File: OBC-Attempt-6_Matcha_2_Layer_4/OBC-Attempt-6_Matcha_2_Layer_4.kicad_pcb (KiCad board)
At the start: 2 copper layers, 57.1 x 57.1 mm, 59 parts, among them J2 Screw_Terminal_01x08, J3 Screw_Terminal_01x08, J5 Conn_01x04, J6 Micro_SD_Card, J7 Screw_Terminal_01x02, J8 Screw_Terminal_01x02, SW1 PCM12SMTR, U1 BMI088, U10 CPC1020NTR, U11 CPC1020NTR, U12 NCP1117-3.3_SOT223, U2 CPC1020NTR, U3 CPC1020NTR, U4 CPC1020NTR, U5 CPC1020NTR, U7 CPC1020NTR, U8 CPC1020NTR, U9 STM32F401RDTx, Y1 ABMM2-25MHZ-D1-T

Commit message: Some Changes
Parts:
- removed D5, D6, D7, D8: B330, Diode_SMD:D_SMA
- removed J3: Screw_Terminal_01x08, TerminalBlock_Phoenix:TerminalBlock_Phoenix_MPT-0,5-8-2.54_1x08_P2.54mm_Horizontal
- removed R14, R15, R16, R17: 270, Resistor_SMD:R_0603_1608Metric
- removed U10, U11, U7, U8: CPC1020NTR, CPC1020NTR:4-SOP
- moved J7 38.9 mm to (29.2, 58.4), turned to 90 degrees
- moved BZ1 36.1 mm to (38.0, 49.9), turned to -45 degrees
- moved J2 33.4 mm to (59.5, 72.4), turned to 180 degrees
- moved D4 30.9 mm to (62.4, 69.1), turned to 180 degrees
- moved D1 30.7 mm to (40.9, 69.0), turned to 180 degrees
- moved D3 27.4 mm to (55.2, 69.1), turned to 180 degrees
- moved D2 27.3 mm to (48.0, 69.1), turned to 180 degrees
- moved U4 25.2 mm to (63.1, 63.5), turned to 180 degrees
- moved U1 23.5 mm to (41.6, 63.4), turned to 180 degrees
- moved J8 23.1 mm to (29.2, 50.8), turned to 90 degrees
- moved Y1 21.8 mm to (39.0, 29.6), turned to -135 degrees
- moved R12 21.7 mm to (64.4, 58.3), turned to 90 degrees
- moved C20 20.3 mm to (26.8, 41.8), turned to 90 degrees
- moved U3 20.2 mm to (56.1, 63.5), turned to 180 degrees
- moved U2 19.5 mm to (48.8, 63.5), turned to 180 degrees
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- renumbered D3 to D2, D4 to D3, D2 to D4, U4 to U1, U5 to U4, U1 to U5, U9 to U6
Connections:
- C20 pad 1: BATT+ -> PWR
- J5 pad 2: 3.3V -> SYS_JTMS-SWDIO
- J5 pad 3: SYS_JTMS-SWDIO -> 3.3V
- J7 pad 1: BATT+ -> GND
- J7 pad 2: GND -> BATT+
- J8 pad 1: PWR -> BATT+
- J8 pad 2: BATT+ -> PWR
- R18 pad 1: BATT+ -> PWR
- U12 pad 3: BATT+ -> PWR
- U6 pad 24: SOL1 -> BUZZER
- U6 pad 25: SOL3 -> unconnected-(U6-Pad25)
- U6 pad 26: SOL2 -> unconnected-(U6-Pad26)
- U6 pad 27: SOL4 -> unconnected-(U6-Pad27)
- U6 pad 41: SOL5 -> SOL1
- U6 pad 42: SOL7 -> SOL2
- U6 pad 43: SOL6 -> SOL3
- U6 pad 44: SOL8 -> SOL4
- U6 pad 56: BUZZER -> unconnected-(U6-Pad56)
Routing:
- net PWR: track 91.8 -> 58.2 mm
- net SOL8: track 22.3 -> 0.00 mm, vias 2 -> 0
- net SOL5: track 22.0 -> 0.00 mm, vias 2 -> 0
- net SOL7: track 18.6 -> 0.00 mm, vias 2 -> 0
- net SOL6: track 16.6 -> 0.00 mm, vias 2 -> 0
- net SOL1: track 10.6 -> 25.2 mm
- net Net-(D8-Pad1): track 8.85 -> 0.00 mm
- net GND: track 57.9 -> 49.3 mm, vias 46 -> 33
- net SOL2: track 11.8 -> 19.8 mm
- net BATT+: track 12.8 -> 5.08 mm
- net Net-(D7-Pad1): track 7.00 -> 0.00 mm
- net Net-(D6-Pad1): track 6.80 -> 0.00 mm
- net VMON: track 20.7 -> 14.1 mm
- net Net-(D5-Pad1): track 6.11 -> 0.00 mm
- net RCC_OSC_OUT: track 5.70 -> 11.3 mm
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- added copper zone on F.Cu, net PWR
- removed copper zone on F.Cu, net BATT+
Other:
- board size 57.1 x 57.1 mm -> 50.8 x 50.8 mm
- board text added: "-BATT IN+"
- board text added: "GND"
- board text added: "MATCHA V2.0"
- board text removed: "+BATT IN-"
- board text removed: "+SOL5-"
- board text removed: "+SOL6-"
- board text removed: "+SOL7-"
- board text removed: "+SOL8-"
- board text removed: "G"
- board text removed: "MATCHA V3.0"

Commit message: PCB LAYOUT
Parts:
- removed BZ1: Buzzer, Buzzer_Beeper:Buzzer_TDK_PS1240P02BT_D12.2mm_H6.5mm
- removed C1, C11, C13, C2, C3, C4, C6, C8, C9: 100nF, Capacitor_SMD:C_0402_1005Metric
- removed C10: 1uF, Capacitor_SMD:C_0603_1608Metric
- removed C15: 4.7uF, Capacitor_SMD:C_0603_1608Metric
- removed C16, C17: 26pf, Capacitor_SMD:C_0402_1005Metric
- removed C20: 100nF, Capacitor_SMD:C_0603_1608Metric
- removed C21: 10uF, Capacitor_SMD:C_0603_1608Metric
- removed C7: 4.7uF, Capacitor_SMD:C_0402_1005Metric
- removed D1, D2, D3, D4: B330, Diode_SMD:D_SMA
- removed H1, H2, H3, H4: MountingHole, MountingHole:MountingHole_3mm
- removed J2: Screw_Terminal_01x08, TerminalBlock_Phoenix:TerminalBlock_Phoenix_MPT-0,5-8-2.54_1x08_P2.54mm_Horizontal
- removed J5: Conn_01x04, Connector_PinHeader_2.54mm:PinHeader_1x04_P2.54mm_Vertical
- removed J6: Micro_SD_Card, Connector_Card:microSD_HC_Wuerth_693072010801
- removed J7, J8: Screw_Terminal_01x02, TerminalBlock_Phoenix:TerminalBlock_Phoenix_MPT-0,5-2-2.54_1x02_P2.54mm_Horizontal
- removed R10, R11, R12, R9: 270, Resistor_SMD:R_0603_1608Metric
- removed R13: 10k, Resistor_SMD:R_0603_1608Metric
- removed R18: 1M, Resistor_SMD:R_0603_1608Metric
- removed R19: 100K, Resistor_SMD:R_0603_1608Metric
- removed SW1: PCM12SMTR, PCM12SMTR:SW_PCM12SMTR
- removed U1, U2, U3, U4: CPC1020NTR, CPC1020NTR:4-SOP
- removed U12: NCP1117-3.3_SOT223, Package_TO_SOT_SMD:SOT-223-3_TabPin2
- removed U5: BMI088, BMI088:BMI088
- removed U6: STM32F401RDTx, Package_QFP:LQFP-64_10x10mm_P0.5mm
- removed Y1: ABMM2-25MHZ-D1-T, ABMM2_6mm_3_6mm:XTAL_ABMM2-25.000MHZ-D1-T
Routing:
- net 3.3V: track 93.2 -> 0.00 mm, vias 4 -> 0
- net PWR: track 58.2 -> 0.00 mm
- net GND: track 49.3 -> 0.00 mm, vias 33 -> 0
- net SDIO_CK: track 29.7 -> 0.00 mm
- net SDIO_D0: track 27.0 -> 0.00 mm
- net SOL1: track 25.2 -> 0.00 mm, vias 2 -> 0
- net SDIO_D3: track 23.8 -> 0.00 mm
- net SDIO_CMD: track 22.7 -> 0.00 mm
- net SOL4: track 22.1 -> 0.00 mm, vias 2 -> 0
- net SDIO_D1: track 21.7 -> 0.00 mm
- net SOL2: track 19.8 -> 0.00 mm, vias 2 -> 0
- net SDIO_D2: track 19.6 -> 0.00 mm
- net MISO: track 19.1 -> 0.00 mm
- net CS2_GYRO: track 19.0 -> 0.00 mm
- net SOL3: track 17.1 -> 0.00 mm, vias 2 -> 0
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- removed copper zone on F.Cu, net 3.3V
- removed copper zone on B.Cu, net GND
- removed copper zone on F.Cu, net GND
- removed copper zone on F.Cu, net PWR
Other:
- board outline removed
- board text removed: "+SOL1-"
- board text removed: "+SOL2-"
- board text removed: "+SOL3-"
- board text removed: "+SOL4-"
- board text removed: "- RCS"
- board text removed: "-BATT IN+"
- board text removed: "3.3"
- board text removed: "ALEX AARHUS"
- board text removed: "ARM"
- board text removed: "BOOT0"
- board text removed: "CLK"
- board text removed: "DIO"
- board text removed: "GND"
- board text removed: "GO KARMAN!"
- board text removed: "GO SAN DIEGO!"
- board text removed: "MATCHA V2.0"
- board text removed: "PSHHHHHHHHH!"
- board text removed: "SDSURP 2023"

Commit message: Complete chematic
Might have to change the optocouplers
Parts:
- added C1: 4.7nF, Capacitor_SMD:C_0402_1005Metric, F.Cu at (157.6, 59.0)
- added C2: 20pF, Capacitor_SMD:C_0402_1005Metric, F.Cu at (159.6, 84.3)
- added C20: 100nF, Capacitor_SMD:C_0603_1608Metric, F.Cu at (139.0, 73.7)
- added C21: 10uF, Capacitor_SMD:C_0603_1608Metric, F.Cu at (145.0, 66.2)
- added C3: 20pF, Capacitor_SMD:C_0402_1005Metric, F.Cu at (159.5, 86.2)
- added C4: 4u7, Capacitor_SMD:C_0402_1005Metric, F.Cu at (165.9, 87.0)
- added C5: 1uF, Capacitor_SMD:C_0402_1005Metric, F.Cu at (166.4, 85.6)
- added C6: .1uF, Capacitor_SMD:C_0402_1005Metric, F.Cu at (136.0, 79.5)
- added C7: 10nF, Capacitor_SMD:C_0402_1005Metric, F.Cu at (152.8, 63.5)
- added D1: CVJ10F30, CVJ10F30:CVJ10F30, F.Cu at (164.4, 39.4)
- added D2: CVJ10F30, CVJ10F30:CVJ10F30, F.Cu at (157.2, 62.1)
- added H1: MountingHole_Pad, MountingHole:MountingHole_2.2mm_M2_Pad_TopBottom, F.Cu at (128.4, 75.5)
- added H2: MountingHole_Pad, MountingHole:MountingHole_2.2mm_M2_Pad_TopBottom, F.Cu at (140.0, 65.0)
- added H3: MountingHole_Pad, MountingHole:MountingHole_2.2mm_M2_Pad_TopBottom, F.Cu at (143.3, 59.0)
- added H4: MountingHole_Pad, MountingHole:MountingHole_2.2mm_M2_Pad_TopBottom, F.Cu at (124.6, 81.4)
- added J1: CAN Header, Connector_PinHeader_1.00mm:PinHeader_1x04_P1.00mm_Vertical, F.Cu at (138.7, 57.5)
- added J2: SOL A, TerminalBlock_Phoenix:TerminalBlock_Phoenix_MPT-0,5-4-2.54_1x04_P2.54mm_Horizontal, F.Cu at (170.0, 44.9)
- added J3: SOL B, TerminalBlock_Phoenix:TerminalBlock_Phoenix_MPT-0,5-4-2.54_1x04_P2.54mm_Horizontal, F.Cu at (103.9, 83.6)
- added J5: Conn_01x04, Connector_PinHeader_2.54mm:PinHeader_1x04_P2.54mm_Vertical, F.Cu at (166.6, 80.9)
- added J7: Screw_Terminal_01x02, TerminalBlock_Phoenix:TerminalBlock_Phoenix_MPT-0,5-2-2.54_1x02_P2.54mm_Horizontal, F.Cu at (116.5, 83.6)
- added J8: Screw_Terminal_01x02, TerminalBlock_Phoenix:TerminalBlock_Phoenix_MPT-0,5-2-2.54_1x02_P2.54mm_Horizontal, F.Cu at (130.1, 68.4)
- added R1: 60 ohm, Resistor_SMD:R_0805_2012Metric, F.Cu at (116.7, 78.0)
- added R10: R, Resistor_SMD:R_0603_1608Metric, F.Cu at (128.0, 85.7)
- added R11: R, Resistor_SMD:R_0603_1608Metric, F.Cu at (149.4, 61.7)
- added R18: 1M, Resistor_SMD:R_0603_1608Metric, F.Cu at (149.4, 64.2)
- added R19: 100K, Resistor_SMD:R_0603_1608Metric, F.Cu at (143.0, 69.3)
- added R2: 60 ohm, Resistor_SMD:R_0805_2012Metric, F.Cu at (145.2, 63.4)
- added R3: 10k, Resistor_SMD:R_0402_1005Metric, F.Cu at (138.5, 76.0)
- added R4: R, Resistor_SMD:R_0402_1005Metric, F.Cu at (144.8, 38.8)
- added R5: R, Resistor_SMD:R_0402_1005Metric, F.Cu at (144.7, 43.8)
- added R6: R, Resistor_SMD:R_0402_1005Metric, F.Cu at (157.6, 57.0)
- added R7: R, Resistor_SMD:R_0402_1005Metric, F.Cu at (142.5, 71.5)
- added R8: R, Resistor_SMD:R_0603_1608Metric, F.Cu at (158.8, 40.4)
- added R9: R, Resistor_SMD:R_0603_1608Metric, F.Cu at (158.8, 45.5)
- added SW1: SW_SPST, Jumper:SolderJumper-2_P1.3mm_Open_RoundedPad1.0x1.5mm, F.Cu at (123.8, 86.2)
- added SW2: SW_SPDT, Jumper:SolderJumper-3_P1.3mm_Open_RoundedPad1.0x1.5mm_NumberLabels, F.Cu at (134.2, 74.3)
- added U1: LTV-827S, Package_DIP:SMDIP-8_W9.53mm, F.Cu at (151.9, 42.5)
- added U12: NCP1117-3.3_SOT223, Package_TO_SOT_SMD:SOT-223-3_TabPin2, F.Cu at (132.1, 60.1)
- added U2: LTV-827S, Package_DIP:SMDIP-8_W9.53mm, F.Cu at (107.9, 73.6)
- added U3: QS5K2TR, QS5K2TR:SOT95P280X100-5N, F.Cu at (161.8, 42.2)
- added U4: QS5K2TR, QS5K2TR:SOT95P280X100-5N, F.Cu at (149.5, 58.2)
- added U5: SN65HVD230, Package_SO:SOIC-8_3.9x4.9mm_P1.27mm, F.Cu at (123.4, 67.5)
- added U6: STM32F042G4Ux, Package_DFN_QFN:QFN-28_4x4mm_P0.5mm, F.Cu at (162.8, 86.0)
- added X1: ECS-2520MV-xxx-xx, Oscillator:Oscillator_SMD_ECS_2520MV-xxx-xx-4Pin_2.5x2.0mm, F.Cu at (157.7, 85.0)
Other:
- board outline added: 50.8 x 50.8 mm

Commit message: Some late night pcb work
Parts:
- removed J7, J8: Screw_Terminal_01x02, TerminalBlock_Phoenix:TerminalBlock_Phoenix_MPT-0,5-2-2.54_1x02_P2.54mm_Horizontal
- removed U2: LTV-827S, Package_DIP:SMDIP-8_W9.53mm
- added J4: Screw_Terminal_01x04, TerminalBlock_Phoenix:TerminalBlock_Phoenix_MPT-0,5-4-2.54_1x04_P2.54mm_Horizontal, B.Cu at (34.2, 29.0)
- D1, D2, J2, J3, R10, R11, R4, R5, R6, R7, R8, R9, U3, U4: moved to B.Cu
- J5: footprint Connector_PinHeader_2.54mm:PinHeader_1x04_P2.54mm_Vertical -> Connector_PinHeader_1.00mm:PinHeader_1x04_P1.00mm_Vertical; moved to B.Cu
- U1: value LTV-827S -> LTV-247; footprint Package_DIP:SMDIP-8_W9.53mm -> Package_SO:SOP-16_4.4x10.4mm_P1.27mm; moved to B.Cu
- moved C1 144.5 mm to (13.9, 43.4), turned to 180 degrees
- moved D1 133.9 mm to (31.3, 54.4), turned to -90 degrees
- moved R2 132.3 mm to (14.7, 41.9)
- moved J2 129.2 mm to (41.7, 60.0), turned to 180 degrees
- moved C4 129.1 mm to (44.0, 44.5)
- moved U3 128.8 mm to (33.3, 51.8), turned to -90 degrees
- moved C5 128.1 mm to (45.0, 44.5), turned to -90 degrees
- moved R8 128.0 mm to (31.1, 48.5), turned to 0 degrees
- moved U6 126.1 mm to (45.0, 40.9), turned to -90 degrees
- moved R9 124.8 mm to (34.1, 48.5), turned to 0 degrees
- moved C3 124.8 mm to (45.0, 36.7), turned to 180 degrees
- moved J5 123.9 mm to (49.5, 40.5), turned to 180 degrees
- moved R6 122.8 mm to (36.1, 38.6), turned to 90 degrees
- moved X1 122.3 mm to (46.2, 34.7), turned to -90 degrees
- moved C2 122.1 mm to (46.7, 37.7), turned to 0 degrees
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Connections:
- U1 pad 5: Net-(R9-Pad2) -> Net-(R6-Pad1)
- U1 pad 6: PWR -> GND
- U1 pad 7: Net-(R8-Pad2) -> Net-(R7-Pad1)
- U1 pad 8: PWR -> GND
- U5 pad 3: +3.3V -> 3.3V
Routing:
- net GND: vias 0 -> 2
- net 3.3V: vias 0 -> 4
- added copper zone on F.Cu, net 3.3V
- added copper zone on In2.Cu, net 3.3V
- added copper zone on F.Cu, net BATT+
- added copper zone on F.Cu, net GND
- added copper zone on In1.Cu, net GND
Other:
- board size 50.8 x 50.8 mm -> 25.4 x 38.1 mm
- copper layers 2 -> 4

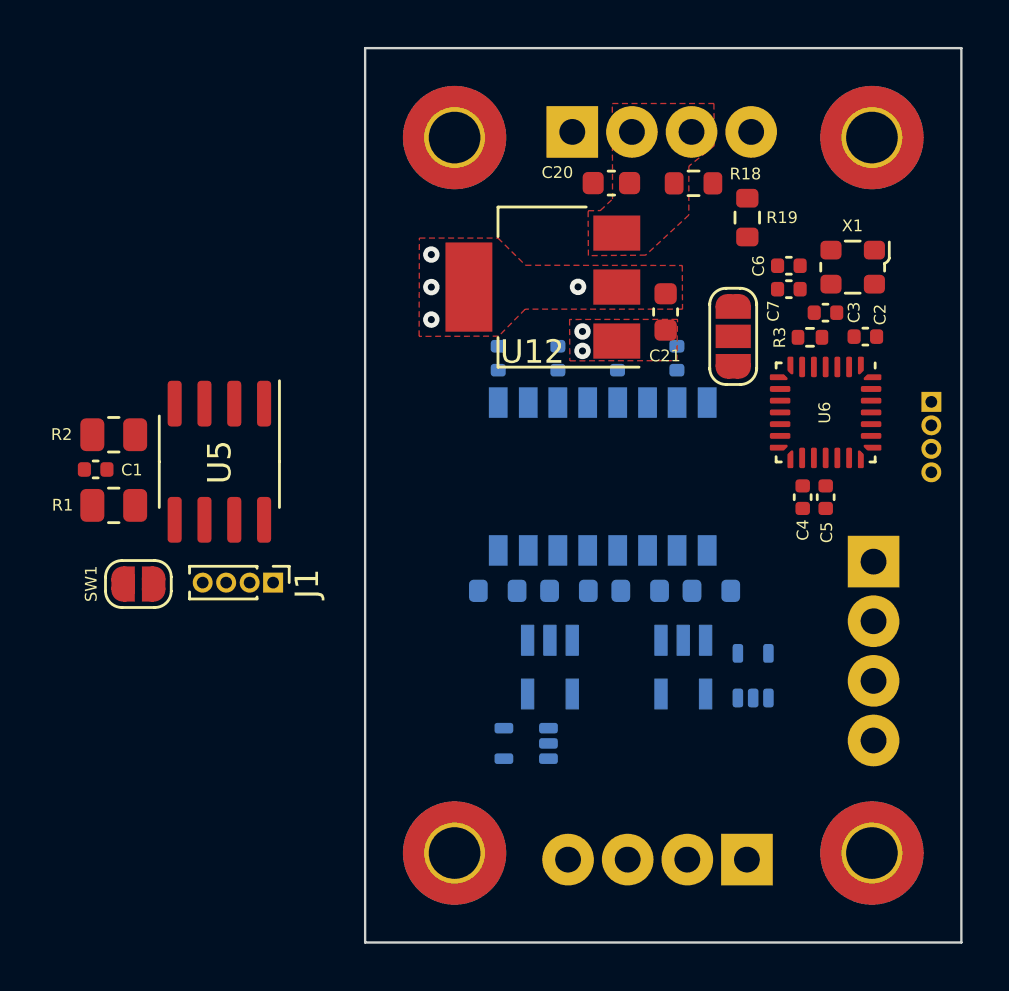
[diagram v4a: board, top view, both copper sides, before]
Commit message: Wired Everything in the board
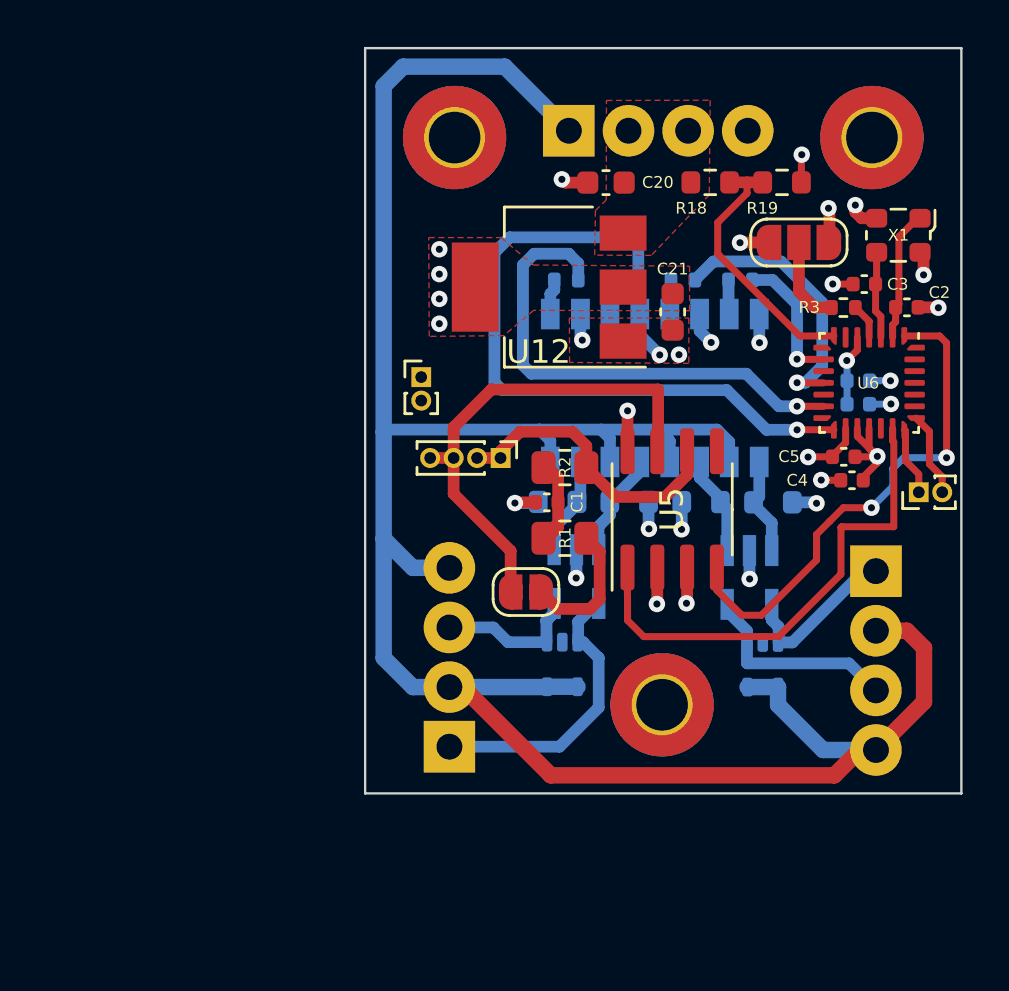
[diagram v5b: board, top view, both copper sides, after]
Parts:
- removed H4: MountingHole_Pad, MountingHole:MountingHole_2.2mm_M2_Pad_TopBottom
- added J6: Conn_01x02_Male, Connector_PinHeader_1.00mm:PinHeader_1x02_P1.00mm_Vertical, F.Cu at (27.8, 39.4)
- C6, C7: moved to B.Cu
- J5: value Conn_01x04 -> Conn_01x02_Male; footprint Connector_PinHeader_1.00mm:PinHeader_1x04_P1.00mm_Vertical -> Connector_PinHeader_1.00mm:PinHeader_1x02_P1.00mm_Vertical; moved to F.Cu
- moved U5 19.4 mm to (38.5, 45.0), turned to 90 degrees
- moved R2 19.3 mm to (33.9, 43.3)
- moved C1 19.3 mm to (33.1, 44.7)
- moved R1 19.3 mm to (33.9, 46.3)
- moved SW1 16.5 mm to (32.2, 48.6), turned to 180 degrees
- moved J2 13.6 mm to (29.0, 55.2), turned to 90 degrees
- moved J1 11.0 mm to (31.2, 42.9)
- moved H3 10.9 mm to (38.0, 53.4)
- moved C6 5.72 mm to (46.4, 39.6), turned to 0 degrees
- moved C7 5.72 mm to (46.4, 40.6), turned to 0 degrees
- moved SW2 4.88 mm to (43.9, 33.7), turned to 0 degrees
- moved U4 4.75 mm to (41.8, 48.0)
- moved R11 4.59 mm to (42.8, 44.8), turned to 180 degrees
- moved R10 4.59 mm to (39.7, 44.7)
- moved R9 4.58 mm to (36.6, 44.7), turned to 180 degrees
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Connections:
- J2 pad 1: PWR -> SOLB
- J2 pad 2: SOLA -> PWR
- J2 pad 3: PWR -> SOLA
- J2 pad 4: SOLB -> PWR
- J3 pad 1: PWR -> SOLD
- J3 pad 2: SOLC -> PWR
- J3 pad 3: PWR -> SOLC
- J3 pad 4: SOLD -> PWR
- J4 pad 1: GND -> PWR
- J4 pad 4: PWR -> GND
- J5 pad 1: SYS_JTCK_SWCLK -> SYS_JTMS-SWDIO
- J5 pad 2: SYS_JTMS-SWDIO -> SYS_JTCK_SWCLK
- U6 pad 11: unconnected-(U6-Pad11) -> SOL3
- U6 pad 13: unconnected-(U6-Pad13) -> SOL1
- U6 pad 15: unconnected-(U6-Pad15) -> SOL2
- U6 pad 7: unconnected-(U6-Pad7) -> VMON
- U6 pad 9: unconnected-(U6-Pad9) -> SOL4
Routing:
- net PWR: track 0.00 -> 101.3 mm
- net GND: track 0.00 -> 29.7 mm, vias 2 -> 24
- net SOL2: track 0.00 -> 28.8 mm, vias 0 -> 1
- net CAN_RX: track 0.00 -> 21.9 mm, vias 0 -> 2
- net SOL1: track 0.00 -> 21.3 mm, vias 0 -> 1
- net CAN_TX: track 0.00 -> 21.2 mm
- net CAN_H: track 0.00 -> 21.1 mm
- net CAN_L: track 0.00 -> 12.7 mm
- net SOLB: track 0.00 -> 12.4 mm
- net SOL3: track 0.00 -> 11.7 mm, vias 0 -> 1
- net VMON: track 0.00 -> 11.4 mm
- net 3.3V: track 0.00 -> 11.2 mm, vias 4 -> 8
- net SOLC: track 0.00 -> 8.83 mm
- net SOLD: track 0.00 -> 7.15 mm
- net SOLA: track 0.00 -> 6.19 mm
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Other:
- board size 25.4 x 38.1 mm -> 25.4 x 31.8 mm
